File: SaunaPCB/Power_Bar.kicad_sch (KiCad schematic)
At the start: 43 parts, among them J200 KL3RM7.62, J201 KL3RM7.62, J202 KL3RM7.62, J203 KL3RM7.62, J204 KL3RM7.62, K201 Relais_SPDT_CO, K202 Relais_SPDT_CO, K203 Relais_SPDT_CO, K204 Relais_SPDT_CO, K205 Relais_SPDT_CO, K206 Relais_SPDT_CO, K207 Relais_SPDT_CO, U201 LHE05-20B24, U202 4N25, U203 4N25, U204 4N25

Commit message: Still working on placement and routing
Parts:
- added R211: 10K, Resistor_SMD:R_1206_3216Metric, symbol Device:R
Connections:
- net N: now also R211.1; no longer D205.2 (A), D206.2 (A), D207.2 (A), U202.2, U203.2, U204.2
- new net: D205.2 (A), D206.2 (A), D207.2 (A), R211.2, U202.2, U203.2, U204.2
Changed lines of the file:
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@@
 	(wire
 		(pts
-			(xy 222.25 105.41) (xy 226.06 105.41)
+			(xy 208.28 106.68) (xy 213.36 106.68)
 		)
 		(stroke
@@
 	(wire
 		(pts
+			(xy 220.98 106.68) (xy 226.06 106.68)
+		)
+		(stroke
+			(width 0)
+			(type default)
+		)
+	)
+	(wire
+		(pts
 			(xy 173.99 124.46) (xy 193.04 124.46)
 		)
@@
 	(wire
 		(pts
-			(xy 226.06 101.6) (xy 226.06 105.41)
+			(xy 226.06 101.6) (xy 226.06 106.68)
 		)
 		(stroke
@@
 	(global_label "N"
 		(shape input)
-		(at 222.25 105.41 180)
+		(at 208.28 106.68 180)
 		(fields_autoplaced yes)
 		(effects
@@
 		)
 		(property "Intersheetrefs" "${INTERSHEET_REFS}"
-			(at 217.9343 105.41 0)
+			(at 203.9643 106.68 0)
 			(effects
 				(font
@@
 					(unit 1)
 				)
+			)
+		)
+	)
+	(symbol
+		(lib_id "Device:R")
+		(at 217.17 106.68 90)
+		(unit 1)
+		(exclude_from_sim no)
+		(in_bom yes)
+		(on_board yes)
+		(dnp no)
+		(property "Reference" "R211"
+			(at 216.916 102.87 90)
+			(effects
+				(font
+					(size 1.27 1.27)
+				)
+			)
+		)
+		(property "Value" "10K"
+			(at 216.916 104.648 90)
+			(effects
+				(font
+					(size 1.27 1.27)
+				)
+			)
+		)
+		(property "Footprint" "Resistor_SMD:R_1206_3216Metric"
+			(at 217.17 108.458 90)
+			(effects
+				(font
+					(size 1.27 1.27)
+				)
+				(hide yes)
+			)
+		)
+		(property "Datasheet" "~"
+			(at 217.17 106.68 0)
+			(effects
+				(font
+					(size 1.27 1.27)
+				)
+				(hide yes)
+			)
+		)
+		(property "Description" "Resistor"
+			(at 217.17 106.68 0)
+			(effects
+				(font
+					(size 1.27 1.27)
+				)
+				(hide yes)
+			)
+		)
+		(pin "1"
+		)
+		(pin "2"
+		)
+		(instances
+			(project "SaunaPCB"
+				(path "/e6d8484d-2bb5-441d-9b2b-e37a9f2fa458/30fa358e-9a57-402a-a6f3-bf544329cd39"
+					(reference "R211")
+					(unit 1)
+				)

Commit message: Still working on placement and routing
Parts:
- added H201, H202, H203, H204, H205: MountingHole, MountingHole:MountingHole_3.2mm_M3_DIN965, symbol Mechanical:MountingHole
- D201, D202, D204: footprint Diode_THT:D_DO-41_SOD81_P10.16mm_Horizontal -> Diode_SMD:D_SMA_Handsoldering
- D203: footprint LED_SMD:LED_PLCC-2_3.4x3.0mm_AK -> Connector_JST:JST_EH_B2B-EH-A_1x02_P2.50mm_Vertical
- R202, R205, R206, R207: footprint Resistor_THT:R_Axial_DIN0207_L6.3mm_D2.5mm_P10.16mm_Horizontal -> Resistor_SMD:R_1206_3216Metric
- R211: footprint Resistor_SMD:R_1206_3216Metric -> Resistor_THT:R_Axial_DIN0207_L6.3mm_D2.5mm_P10.16mm_Horizontal

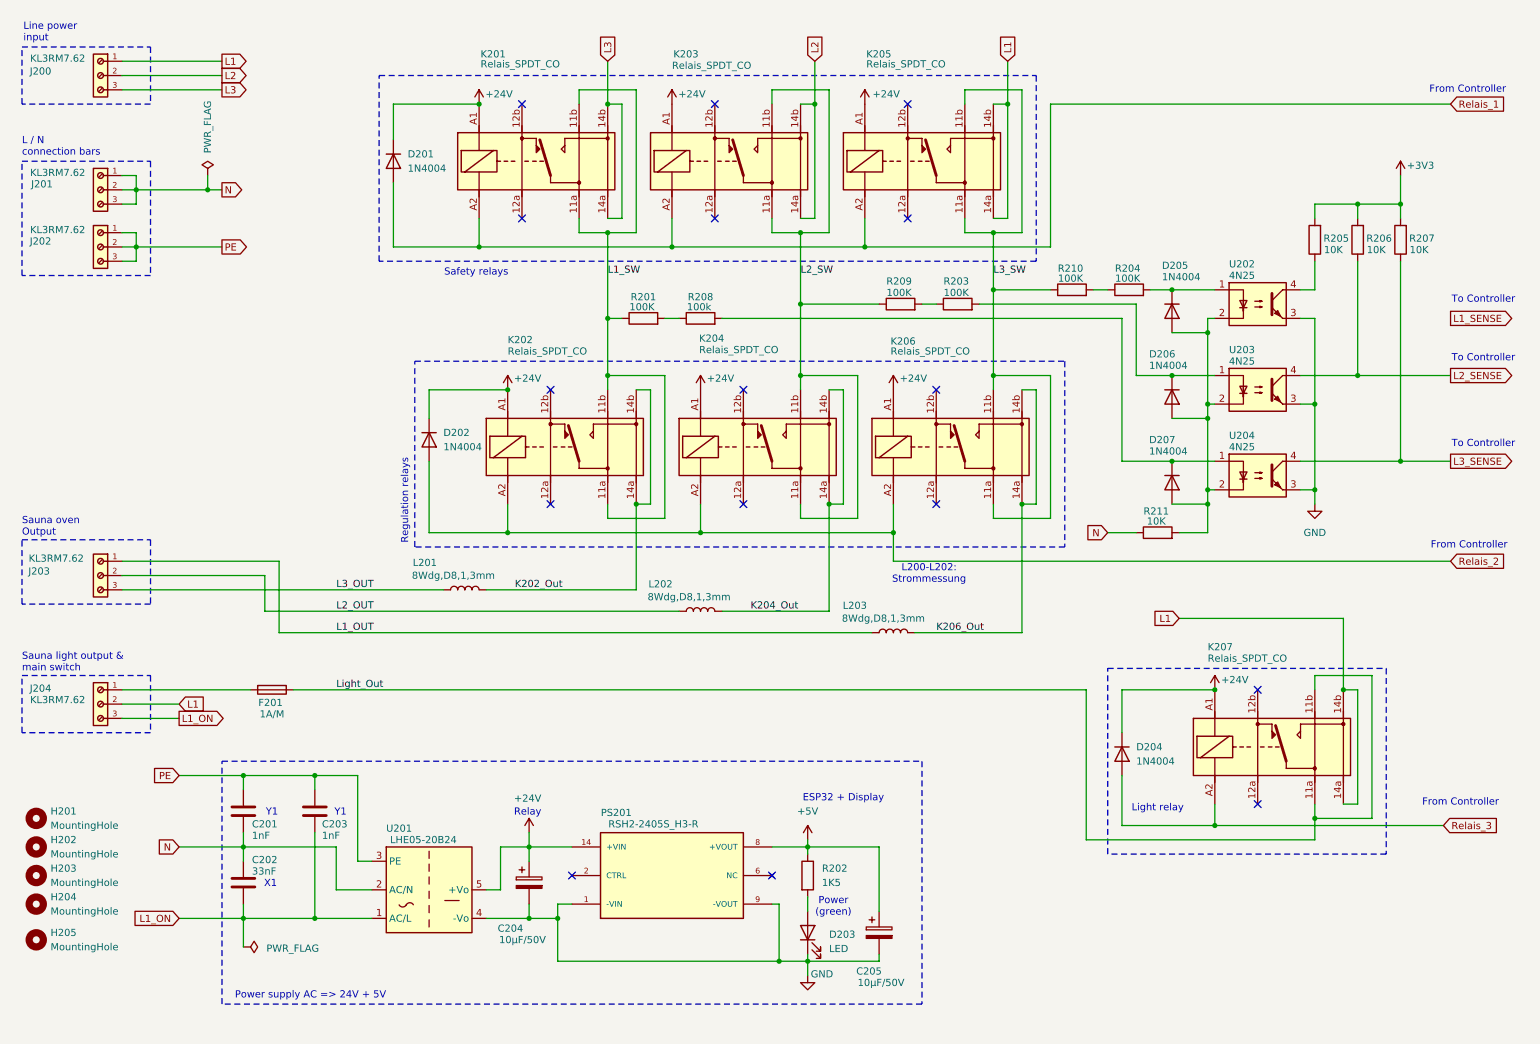
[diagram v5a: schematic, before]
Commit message: Relay power supply changed
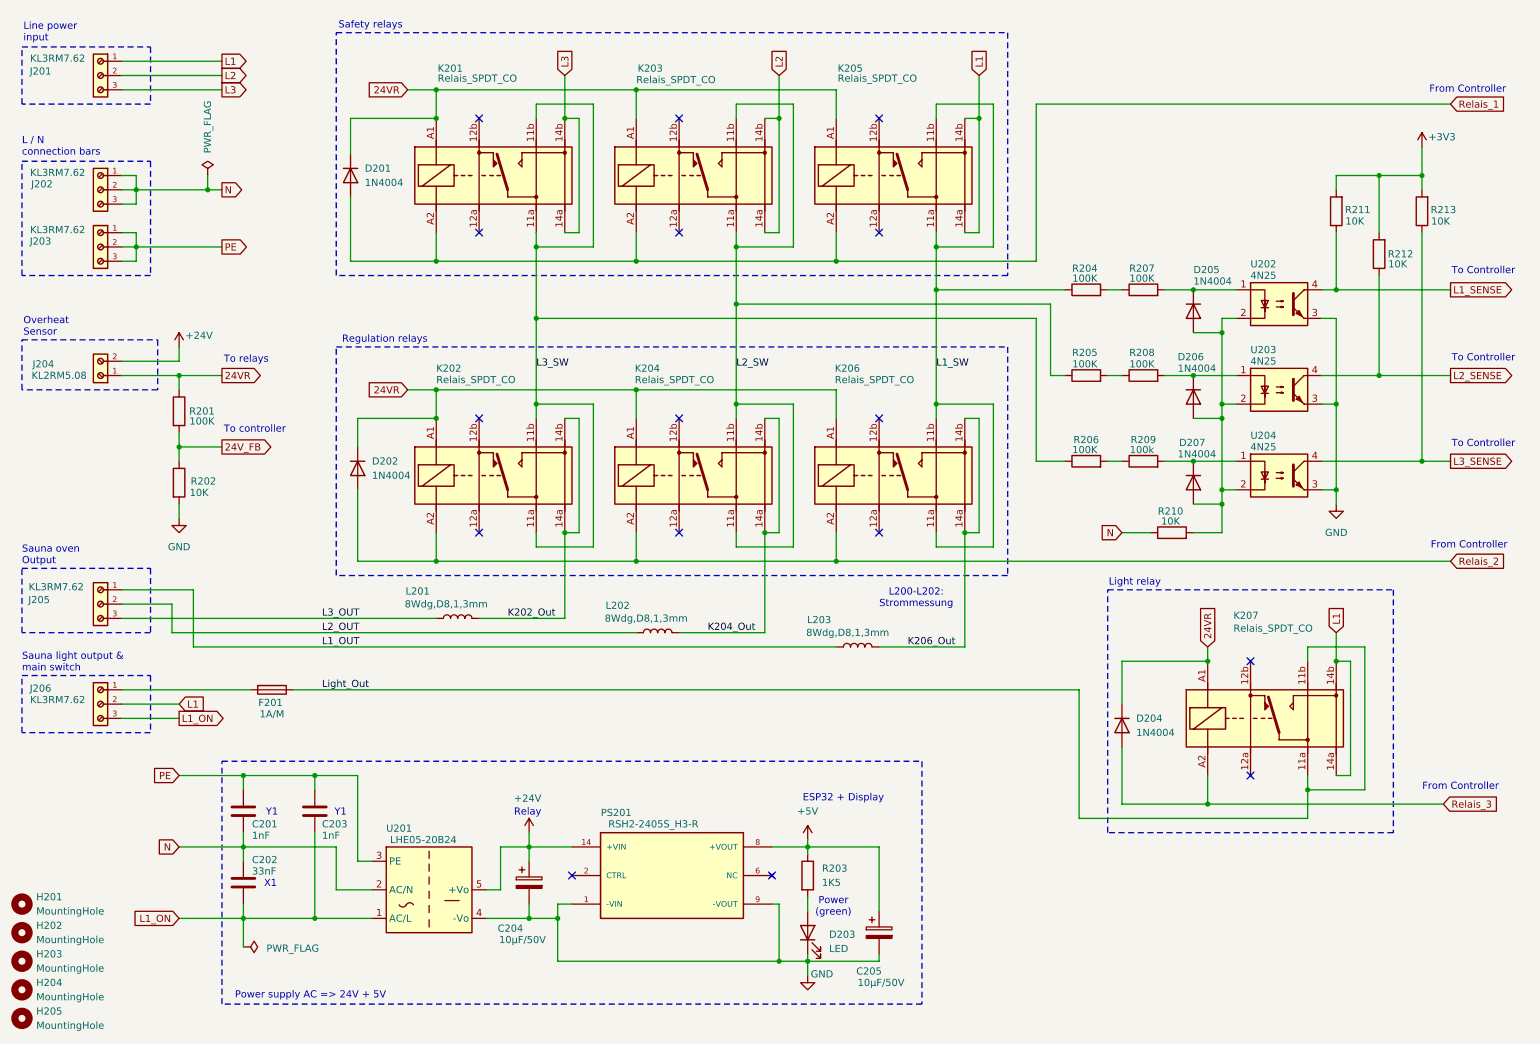
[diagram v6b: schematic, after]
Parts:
- added J204: KL2RM5.08, MyConnectors:Terminal_Block_2_RM5.08, symbol MyConnectors:Terminal_Block_2
- added R201: 100K, Resistor_SMD:R_1206_3216Metric, symbol Device:R
- added R202: 10K, Resistor_SMD:R_1206_3216Metric, symbol Device:R
- renumbered J200 to J201, J201 to J202, J202 to J203, J203 to J205, J204 to J206, R202 to R203, R210 to R204, R209 to R205, R201 to R206, R204 to R207, R203 to R208, R208 to R209, R211 to R210, R205 to R211, R206 to R212, R207 to R213
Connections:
- net +24V: now also J204.2; no longer D201.1 (K), D202.1 (K), D204.1 (K), K201.A1, K202.A1, K203.A1, K204.A1, K205.A1, K206.A1, K207.A1
- net GND: now also R202.2
- net L1_SENSE: now also R211.1, U202.4
- net L1_SW: now also K205.11a, K205.11b, K206.11a, K206.11b, R204.1; no longer K201.11a, K201.11b, K202.11a, K202.11b, R206.1
- net L3_SW: now also K201.11a, K201.11b, K202.11a, K202.11b, R206.1; no longer K205.11a, K205.11b, K206.11a, K206.11b, R204.1
- new net 24VR: D201.1 (K), D202.1 (K), D204.1 (K), J204.1, K201.A1, K202.A1, K203.A1, K204.A1, K205.A1, K206.A1, K207.A1, R201.1
- new net 24V_FB: R201.2, R202.1
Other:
- note added: "Overheat Sensor"
- note added: "To controller"
- note added: "To relays"
- moved on the sheet: D201, D202, D204, D205, D206, D207, H201, H202, H203, H204, H205, J205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

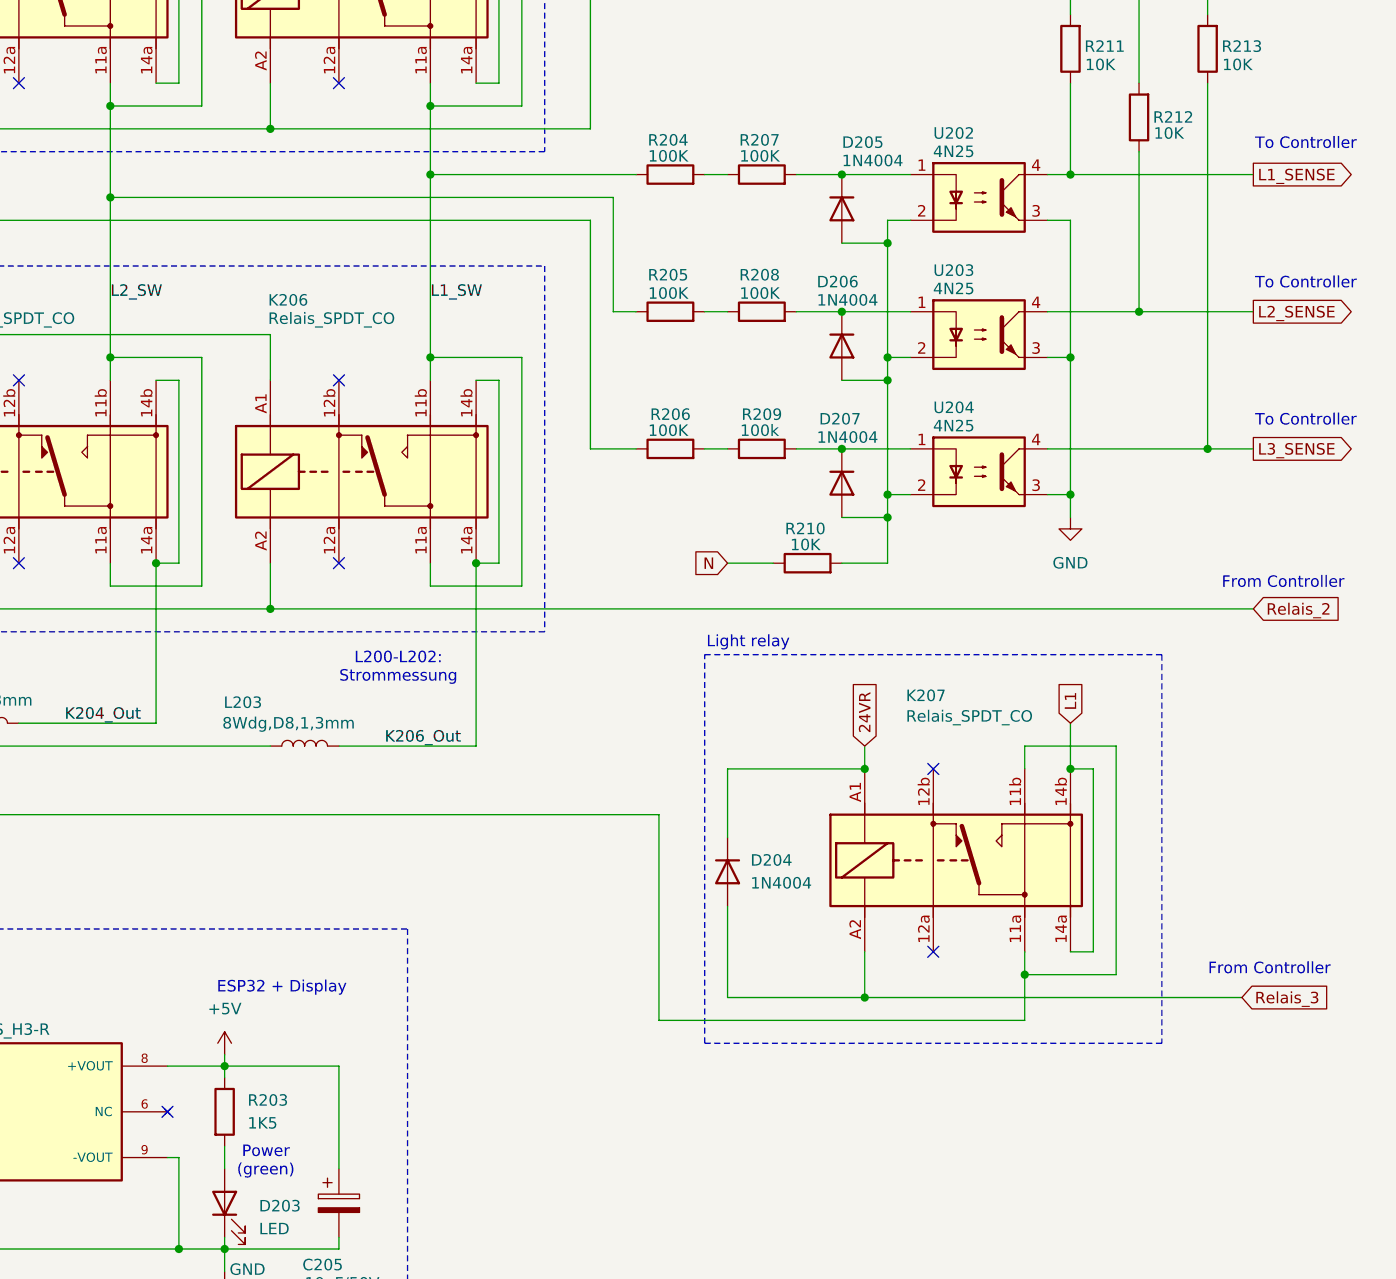
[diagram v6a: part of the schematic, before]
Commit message: Working on schematic: - Own ESP32 Devkit V4 device used. - ESP32 connections added (all signals from page on connected)
- Next steps: Connection to LCD, Relay driver, Encoder Interface and standby LED
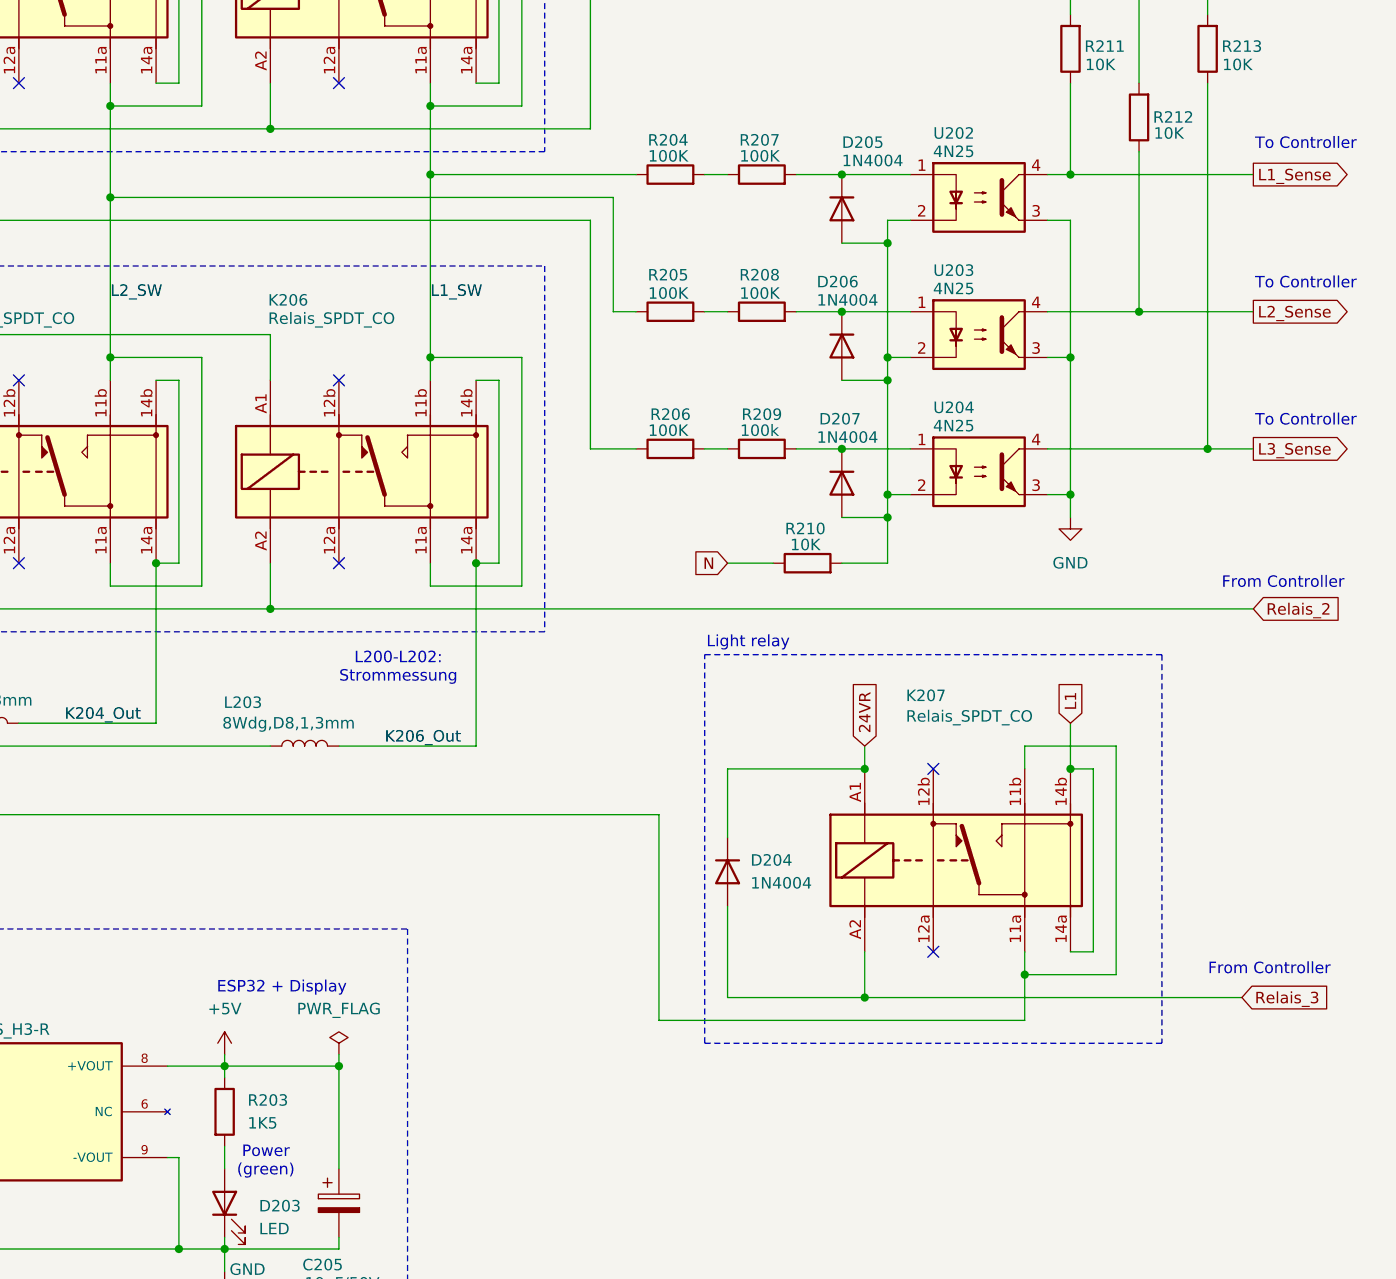
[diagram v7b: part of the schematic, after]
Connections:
- net L1_SENSE renamed L1_Sense
- net L2_SENSE renamed L2_Sense
- net L3_SENSE renamed L3_Sense
- no-connect marks 16 -> 15
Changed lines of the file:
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@@
 	)
 	(junction
+		(at 167.64 162.56)
+		(diameter 0)
+		(color 0 0 0 0)
+	)
+	(junction
 		(at 264.16 93.98)
 		(diameter 0)
@@
 	)
 	(no_connect
-		(at 148.59 167.64)
-	)
-	(no_connect
 		(at 113.03 167.64)
 	)
@@
 	(wire
 		(pts
+			(xy 167.64 161.29) (xy 167.64 162.56)
+		)
+		(stroke
+			(width 0)
+			(type default)
+		)
+	)
+	(wire
+		(pts
 			(xy 124.46 81.28) (xy 124.46 86.36)
 		)
@@
 		)
 	)
-	(global_label "L2_SENSE"
+	(global_label "L2_Sense"
 		(shape output)
 		(at 269.24 78.74 0)
@@
 		)
 		(property "Intersheetrefs" "${INTERSHEET_REFS}"
-			(at 281.4779 78.74 0)
+			(at 280.9942 78.74 0)
 			(effects
 				(font
@@
 		)
 	)
-	(global_label "L3_SENSE"
+	(global_label "L3_Sense"
 		(shape output)
 		(at 269.24 93.98 0)
@@
 		)
 		(property "Intersheetrefs" "${INTERSHEET_REFS}"
-			(at 281.4779 93.98 0)
+			(at 280.9942 93.98 0)
 			(effects
 				(font
@@
 		)
 	)
-	(global_label "L1_SENSE"
+	(global_label "L1_Sense"
 		(shape output)
 		(at 269.24 63.5 0)
@@
 		)
 		(property "Intersheetrefs" "${INTERSHEET_REFS}"
-			(at 281.4779 63.5 0)
+			(at 280.9942 63.5 0)
 			(effects
 				(font
@@
 					(unit 1)
 				)
+			)
+		)
+	)
+	(symbol
+		(lib_id "power:PWR_FLAG")
+		(at 167.64 161.29 0)
+		(unit 1)
+		(exclude_from_sim no)
+		(in_bom yes)
+		(on_board yes)
+		(dnp no)
+		(fields_autoplaced yes)
+		(property "Reference" "#FLG0302"
+			(at 167.64 159.385 0)
+			(effects
+				(font
+					(size 1.27 1.27)
+				)
+				(hide yes)
+			)
+		)
+		(property "Value" "PWR_FLAG"
+			(at 167.64 156.21 0)
+			(effects
+				(font
+					(size 1.27 1.27)
+				)
+			)
+		)
+		(property "Footprint" ""
+			(at 167.64 161.29 0)
+			(effects
+				(font
+					(size 1.27 1.27)
+				)
+				(hide yes)
+			)
+		)
+		(property "Datasheet" "~"
+			(at 167.64 161.29 0)
+			(effects
+				(font
+					(size 1.27 1.27)
+				)
+				(hide yes)
+			)
+		)
+		(property "Description" "Special symbol for telling ERC where power comes from"
+			(at 167.64 161.29 0)
+			(effects
+				(font
+					(size 1.27 1.27)
+				)
+				(hide yes)
+			)
+		)
+		(pin "1"
+		)
+		(instances
+			(project ""
+				(path "/e6d8484d-2bb5-441d-9b2b-e37a9f2fa458/30fa358e-9a57-402a-a6f3-bf544329cd39"
+					(reference "#FLG0302")
+					(unit 1)
+				)
